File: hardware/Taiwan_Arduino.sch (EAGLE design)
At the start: 44 parts, among them J1 AVR_SPI_PRG_62X3_LOCK, T1 2SC, T2 2N, U1 ATMEGA328P_PDIP, Y2 16mhz

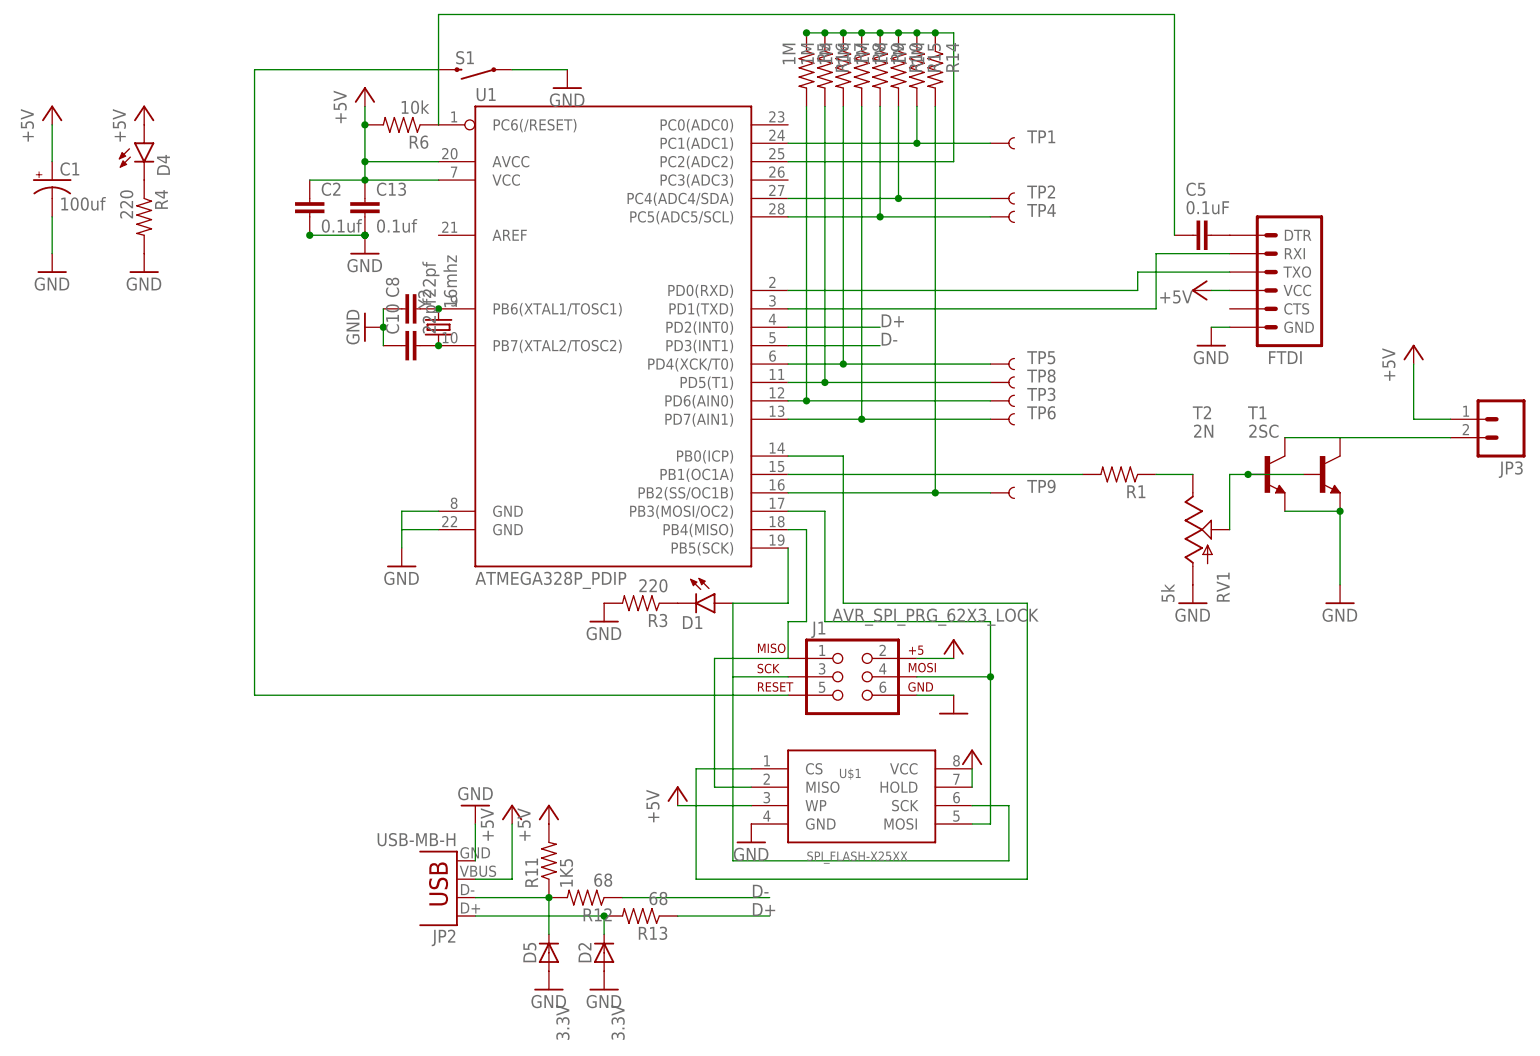
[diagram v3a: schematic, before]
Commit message: Improve touch pad grounding
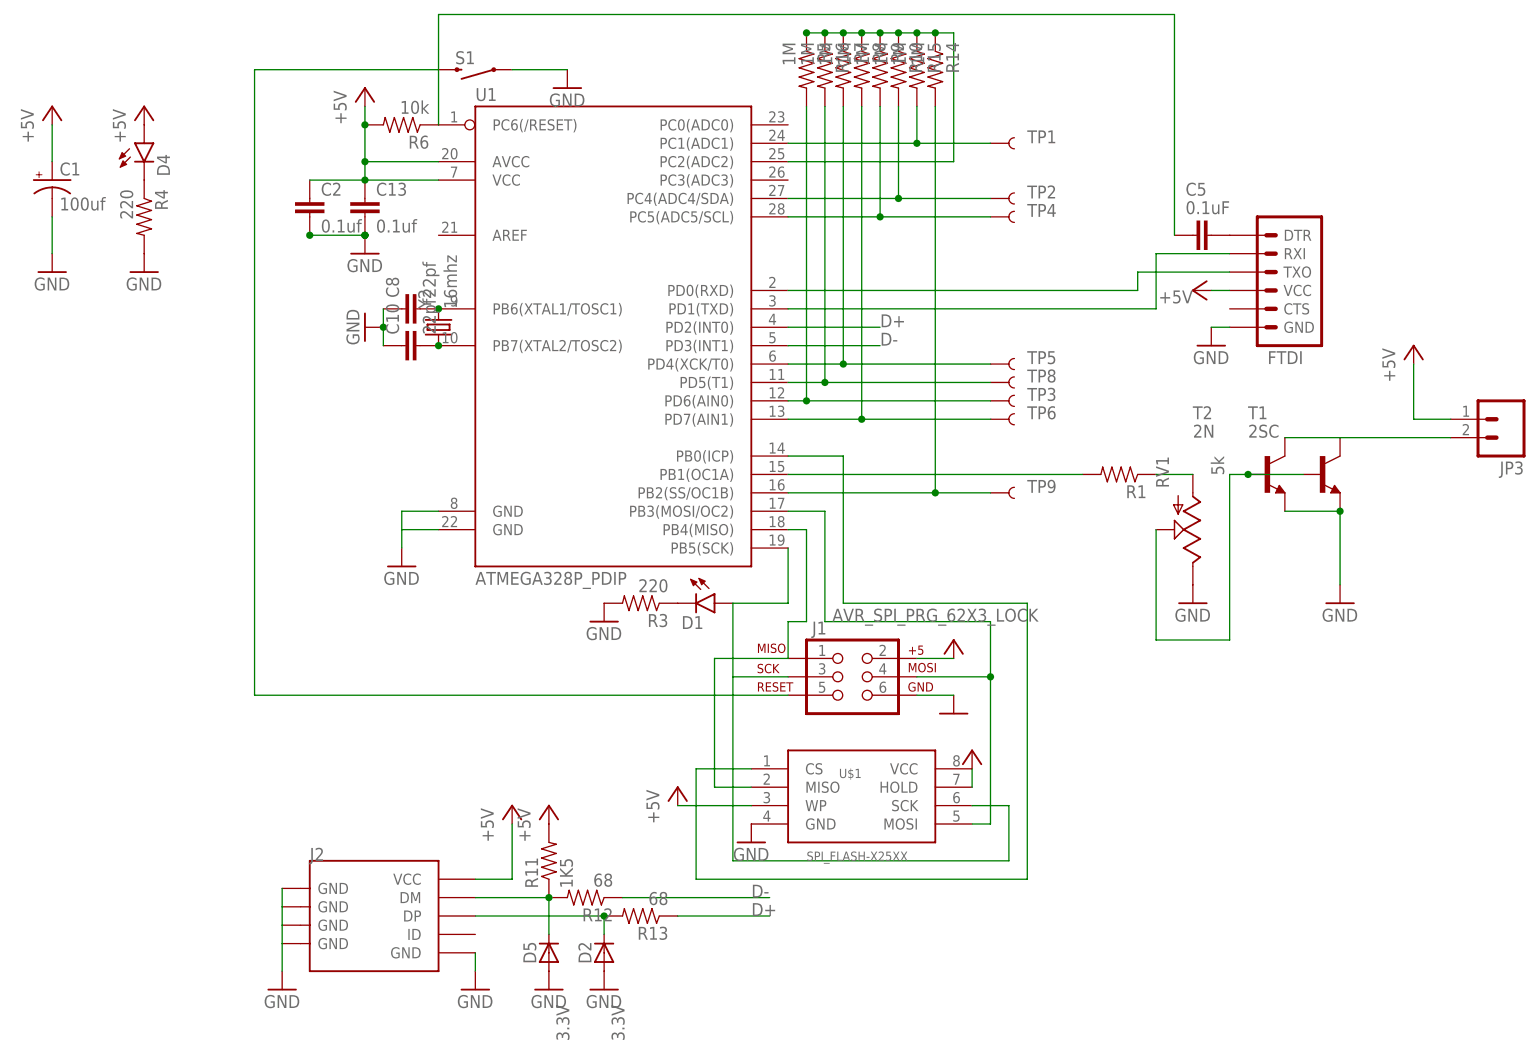
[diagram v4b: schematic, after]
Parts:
- removed JP2: USB-MB-H, SparkFun-Connectors:USB-MB-H
- added J2: (no value), Connector :USB-MINIUSB-5P-TH
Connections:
- net +5V: now also J2.VCC; no longer JP2.VBUS
- net GND: now also J2.GND@1, J2.GND@2, J2.GND@3, J2.GND@4, J2.GND@5, RV1.E; no longer JP2.GND, RV1.A
- net N$1: now also RV1.A; no longer RV1.E
- net N$15: now also J2.DM; no longer JP2.D-
- net N$16: now also J2.DP; no longer JP2.D+
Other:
- moved on the sheet: RV1
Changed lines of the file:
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@@
 <setting verticaltext="up"/>
 </settings>
-<grid distance="0.1" unitdist="inch" unit="inch" style="lines" multiple="1" display="no" altdistance="0.01" altunitdist="inch" altunit="inch"/>
+<grid distance="0.05" unitdist="inch" unit="inch" style="lines" multiple="1" display="no" altdistance="0.01" altunitdist="inch" altunit="inch"/>
 <layers>
 <layer number="1" name="Top" color="4" fill="1" visible="yes" active="no"/>
@@
 <part name="P+11" library="supply1" deviceset="+5V" device=""/>
 <part name="GND22" library="supply1" deviceset="GND" device=""/>
-<part name="JP2" library="SparkFun-Connectors" deviceset="USB" device="-MB-H"/>
 <part name="GND4" library="supply1" deviceset="GND" device=""/>
 <part name="C13" library="SparkFun-Capacitors" deviceset="CAP" device="PTH" value="0.1uf"/>
@@
 <part name="D5" library="_JJG-parts" deviceset="DIODE-VERT" device="DIODE_SM_VERT" value="3.3V"/>
 <part name="D2" library="_JJG-parts" deviceset="DIODE-VERT" device="DIODE_SM_VERT" value="3.3V"/>
+<part name="J2" library="Connector " deviceset="USB-MINIUSB-5P" device="-TH"/>
+<part name="GND1" library="supply1" deviceset="GND" device=""/>
 </parts>
 <sheets>
@@
 <instance part="GND15" gate="1" x="60.96" y="12.7"/>
 <instance part="P+11" gate="1" x="48.26" y="38.1"/>
-<instance part="GND22" gate="1" x="43.18" y="38.1" rot="R180"/>
-<instance part="JP2" gate="G$1" x="40.64" y="30.48" rot="R180"/>
+<instance part="GND22" gate="1" x="43.18" y="12.7"/>
 <instance part="GND4" gate="1" x="33.02" y="71.12"/>
 <instance part="C13" gate="G$1" x="27.94" y="119.38"/>
@@
 <instance part="GND3" gate="1" x="162.56" y="66.04"/>
 <instance part="P+1" gate="1" x="172.72" y="101.6"/>
-<instance part="RV1" gate="G$1" x="142.24" y="76.2"/>
+<instance part="RV1" gate="G$1" x="142.24" y="76.2" rot="R180"/>
 <instance part="GND6" gate="1" x="142.24" y="66.04"/>
 <instance part="U$1" gate="G$1" x="96.52" y="40.64" smashed="yes">
@@
 <attribute name="VALUE" x="63.7794" y="5.588" size="1.778" layer="96" rot="R90"/>
 </instance>
+<instance part="J2" gate="USB" x="29.21" y="22.86"/>
+<instance part="GND1" gate="1" x="16.51" y="12.7"/>
 </instances>
 <busses>
@@
 <nets>
 <net name="GND" class="0">
-<segment>
-<pinref part="GND22" gate="1" pin="GND"/>
-<wire x1="43.18" y1="35.56" x2="43.18" y2="30.48" width="0.1524" layer="91"/>
-<pinref part="JP2" gate="G$1" pin="GND"/>
-</segment>
 <segment>
 <pinref part="C13" gate="G$1" pin="2"/>
@@
 </segment>
 <segment>
-<pinref part="RV1" gate="G$1" pin="A"/>
-<pinref part="GND6" gate="1" pin="GND"/>
-</segment>
-<segment>
 <pinref part="R4" gate="G$1" pin="2"/>
 <pinref part="GND11" gate="1" pin="GND"/>
@@
 <pinref part="D2" gate="1" pin="A"/>
 </segment>
+<segment>
+<pinref part="J2" gate="USB" pin="GND@5"/>
+<pinref part="GND22" gate="1" pin="GND"/>
+<wire x1="43.18" y1="15.24" x2="43.18" y2="17.78" width="0.1524" layer="91"/>
+</segment>
+<segment>
+<pinref part="J2" gate="USB" pin="GND@1"/>
+<pinref part="J2" gate="USB" pin="GND@2"/>
+<wire x1="16.51" y1="26.67" x2="16.51" y2="24.13" width="0.1524" layer="91"/>
+<pinref part="J2" gate="USB" pin="GND@3"/>
+<wire x1="16.51" y1="24.13" x2="16.51" y2="21.59" width="0.1524" layer="91"/>
+<pinref part="J2" gate="USB" pin="GND@4"/>
+<wire x1="16.51" y1="21.59" x2="16.51" y2="19.05" width="0.1524" layer="91"/>
+<pinref part="GND1" gate="1" pin="GND"/>
+<wire x1="16.51" y1="19.05" x2="16.51" y2="15.24" width="0.1524" layer="91"/>
+</segment>
+<segment>
+<pinref part="RV1" gate="G$1" pin="E"/>
+<pinref part="GND6" gate="1" pin="GND"/>
+</segment>
 </net>
 <net name="+5V" class="0">
@@
 <wire x1="43.18" y1="27.94" x2="48.26" y2="27.94" width="0.1524" layer="91"/>
 <wire x1="48.26" y1="27.94" x2="48.26" y2="35.56" width="0.1524" layer="91"/>
-<pinref part="JP2" gate="G$1" pin="VBUS"/>
+<pinref part="J2" gate="USB" pin="VCC"/>
 </segment>
 <segment>
@@
 <junction x="53.34" y="25.4"/>
 <pinref part="R12" gate="G$1" pin="2"/>
-<pinref part="JP2" gate="G$1" pin="D-"/>
 <pinref part="D5" gate="1" pin="C"/>
+<pinref part="J2" gate="USB" pin="DM"/>
 </segment>
 </net>
@@
 <pinref part="R13" gate="G$1" pin="2"/>
 <junction x="60.96" y="22.86"/>
-<pinref part="JP2" gate="G$1" pin="D+"/>
 <pinref part="D2" gate="1" pin="C"/>
+<pinref part="J2" gate="USB" pin="DP"/>
 </segment>
 </net>
@@
 </segment>
 </net>
-<net name="N$1" class="0">
-<segment>
-<pinref part="R1" gate="G$1" pin="1"/>
-<pinref part="RV1" gate="G$1" pin="E"/>
-<wire x1="137.16" y1="83.82" x2="142.24" y2="83.82" width="0.1524" layer="91"/>
-</segment>
-</net>
 <net name="N$2" class="0">
 <segment>
@@
 <net name="N$22" class="0">
 <segment>
-<pinref part="RV1" gate="G$1" pin="S"/>
-<wire x1="147.32" y1="76.2" x2="147.32" y2="83.82" width="0.1524" layer="91"/>
 <pinref part="T1" gate="G$1" pin="B"/>
 <wire x1="157.48" y1="83.82" x2="149.86" y2="83.82" width="0.1524" layer="91"/>
@@
 <wire x1="149.86" y1="83.82" x2="147.32" y2="83.82" width="0.1524" layer="91"/>
 <junction x="149.86" y="83.82"/>
+<wire x1="147.32" y1="83.82" x2="147.32" y2="60.96" width="0.1524" layer="91"/>
+<pinref part="RV1" gate="G$1" pin="S"/>
+<wire x1="147.32" y1="60.96" x2="137.16" y2="60.96" width="0.1524" layer="91"/>
+<wire x1="137.16" y1="60.96" x2="137.16" y2="76.2" width="0.1524" layer="91"/>
 </segment>
 </net>
@@
 </segment>
 </net>
+<net name="N$1" class="0">
+<segment>
+<pinref part="R1" gate="G$1" pin="1"/>
+<pinref part="RV1" gate="G$1" pin="A"/>
+<wire x1="142.24" y1="83.82" x2="137.16" y2="83.82" width="0.1524" layer="91"/>
+</segment>
+</net>

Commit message: Ver 1.0
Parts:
- removed T1: 2SC, transistor:2SC1815
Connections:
- removed net N$18: JP3.2, T1.C, T2.C
- new net N$12: JP3.1, T2.C
- net +5V: now also JP3.2; no longer JP3.1
- net GND: no longer T1.E
- net N$22: no longer T1.B
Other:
- moved on the sheet: JP3
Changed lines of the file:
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@@
 <setting verticaltext="up"/>
 </settings>
-<grid distance="0.05" unitdist="inch" unit="inch" style="lines" multiple="1" display="no" altdistance="0.01" altunitdist="inch" altunit="inch"/>
+<grid distance="0.1" unitdist="inch" unit="inch" style="lines" multiple="1" display="no" altdistance="0.01" altunitdist="inch" altunit="inch"/>
 <layers>
-<layer number="1" name="Top" color="4" fill="1" visible="yes" active="no"/>
-<layer number="16" name="Bottom" color="1" fill="1" visible="yes" active="no"/>
-<layer number="17" name="Pads" color="2" fill="1" visible="yes" active="no"/>
-<layer number="18" name="Vias" color="2" fill="1" visible="yes" active="no"/>
-<layer number="19" name="Unrouted" color="6" fill="1" visible="yes" active="no"/>
-<layer number="20" name="Dimension" color="15" fill="1" visible="yes" active="no"/>
-<layer number="21" name="tPlace" color="7" fill="1" visible="yes" active="no"/>
-<layer number="22" name="bPlace" color="7" fill="1" visible="yes" active="no"/>
-<layer number="23" name="tOrigins" color="15" fill="1" visible="yes" active="no"/>
-<layer number="24" name="bOrigins" color="15" fill="1" visible="yes" active="no"/>
-<layer number="25" name="tNames" color="7" fill="1" visible="yes" active="no"/>
-<layer number="26" name="bNames" color="7" fill="1" visible="yes" active="no"/>
-<layer number="27" name="tValues" color="7" fill="1" visible="yes" active="no"/>
-<layer number="28" name="bValues" color="7" fill="1" visible="yes" active="no"/>
+<layer number="1" name="Top" color="4" fill="1" visible="no" active="no"/>
+<layer number="16" name="Bottom" color="1" fill="1" visible="no" active="no"/>
+<layer number="17" name="Pads" color="2" fill="1" visible="no" active="no"/>
+<layer number="18" name="Vias" color="2" fill="1" visible="no" active="no"/>
+<layer number="19" name="Unrouted" color="6" fill="1" visible="no" active="no"/>
+<layer number="20" name="Dimension" color="15" fill="1" visible="no" active="no"/>
+<layer number="21" name="tPlace" color="7" fill="1" visible="no" active="no"/>
+<layer number="22" name="bPlace" color="7" fill="1" visible="no" active="no"/>
+<layer number="23" name="tOrigins" color="15" fill="1" visible="no" active="no"/>
+<layer number="24" name="bOrigins" color="15" fill="1" visible="no" active="no"/>
+<layer number="25" name="tNames" color="7" fill="1" visible="no" active="no"/>
+<layer number="26" name="bNames" color="7" fill="1" visible="no" active="no"/>
+<layer number="27" name="tValues" color="7" fill="1" visible="no" active="no"/>
+<layer number="28" name="bValues" color="7" fill="1" visible="no" active="no"/>
 <layer number="29" name="tStop" color="7" fill="3" visible="no" active="no"/>
 <layer number="30" name="bStop" color="7" fill="6" visible="no" active="no"/>
@@
 <layer number="35" name="tGlue" color="7" fill="4" visible="no" active="no"/>
 <layer number="36" name="bGlue" color="7" fill="5" visible="no" active="no"/>
-<layer number="37" name="tTest" color="7" fill="1" visible="yes" active="no"/>
-<layer number="38" name="bTest" color="7" fill="1" visible="yes" active="no"/>
+<layer number="37" name="tTest" color="7" fill="1" visible="no" active="no"/>
+<layer number="38" name="bTest" color="7" fill="1" visible="no" active="no"/>
 <layer number="39" name="tKeepout" color="4" fill="11" visible="no" active="no"/>
 <layer number="40" name="bKeepout" color="1" fill="11" visible="no" active="no"/>
@@
 <layer number="44" name="Drills" color="7" fill="1" visible="no" active="no"/>
 <layer number="45" name="Holes" color="7" fill="1" visible="no" active="no"/>
-<layer number="46" name="Milling" color="3" fill="1" visible="yes" active="no"/>
-<layer number="47" name="Measures" color="7" fill="1" visible="yes" active="no"/>
-<layer number="48" name="Document" color="7" fill="1" visible="yes" active="no"/>
-<layer number="49" name="Reference" color="7" fill="1" visible="yes" active="no"/>
-<layer number="50" name="dxf" color="7" fill="1" visible="yes" active="no"/>
-<layer number="51" name="tDocu" color="7" fill="1" visible="yes" active="no"/>
-<layer number="52" name="bDocu" color="7" fill="1" visible="yes" active="no"/>
-<layer number="53" name="tGND_GNDA" color="7" fill="9" visible="yes" active="no"/>
-<layer number="54" name="bGND_GNDA" color="1" fill="9" visible="yes" active="no"/>
-<layer number="56" name="wert" color="7" fill="1" visible="yes" active="no"/>
-<layer number="57" name="tCAD" color="7" fill="1" visible="yes" active="no"/>
-<layer number="59" name="tCarbon" color="7" fill="1" visible="yes" active="no"/>
-<layer number="60" name="bCarbon" color="7" fill="1" visible="yes" active="no"/>
+<layer number="46" name="Milling" color="3" fill="1" visible="no" active="no"/>
+<layer number="47" name="Measures" color="7" fill="1" visible="no" active="no"/>
+<layer number="48" name="Document" color="7" fill="1" visible="no" active="no"/>
+<layer number="49" name="Reference" color="7" fill="1" visible="no" active="no"/>
+<layer number="50" name="dxf" color="7" fill="1" visible="no" active="no"/>
+<layer number="51" name="tDocu" color="7" fill="1" visible="no" active="no"/>
+<layer number="52" name="bDocu" color="7" fill="1" visible="no" active="no"/>
+<layer number="53" name="tGND_GNDA" color="7" fill="9" visible="no" active="no"/>
+<layer number="54" name="bGND_GNDA" color="1" fill="9" visible="no" active="no"/>
+<layer number="56" name="wert" color="7" fill="1" visible="no" active="no"/>
+<layer number="57" name="tCAD" color="7" fill="1" visible="no" active="no"/>
+<layer number="59" name="tCarbon" color="7" fill="1" visible="no" active="no"/>
+<layer number="60" name="bCarbon" color="7" fill="1" visible="no" active="no"/>
 <layer number="90" name="Modules" color="5" fill="1" visible="yes" active="yes"/>
 <layer number="91" name="Nets" color="2" fill="1" visible="yes" active="yes"/>
@@
 <part name="P+8" library="supply1" deviceset="+5V" device=""/>
 <part name="GND18" library="supply1" deviceset="GND" device=""/>
-<part name="T1" library="transistor" deviceset="2SC1815" device="" value="2SC"/>
 <part name="T2" library="adafruit" deviceset="2N2222" device="" value="2N"/>
 <part name="C1" library="adafruit" deviceset="CPOL-US" device="E2.5-5" value="100uf"/>
@@
 <instance part="GND14" gate="1" x="81.28" y="33.02"/>
 <instance part="P+7" gate="1" x="71.12" y="40.64"/>
-<instance part="JP3" gate="G$1" x="185.42" y="91.44" smashed="yes" rot="R180">
-<attribute name="NAME" x="187.96" y="85.598" size="1.778" layer="95" rot="R180"/>
+<instance part="JP3" gate="G$1" x="165.1" y="88.9" smashed="yes">
+<attribute name="NAME" x="162.56" y="94.742" size="1.778" layer="95"/>
 </instance>
 <instance part="R5" gate="G$1" x="88.9" y="139.7" rot="R270"/>
@@
 <instance part="P+8" gate="1" x="-15.24" y="134.62"/>
 <instance part="GND18" gate="1" x="-15.24" y="111.76"/>
-<instance part="T1" gate="G$1" x="160.02" y="83.82"/>
 <instance part="T2" gate="G$1" x="152.4" y="83.82"/>
 <instance part="C1" gate="G$1" x="-15.24" y="124.46"/>
@@
 </segment>
 <segment>
-<pinref part="T1" gate="G$1" pin="E"/>
 <wire x1="154.94" y1="78.74" x2="162.56" y2="78.74" width="0.1524" layer="91"/>
 <pinref part="GND3" gate="1" pin="GND"/>
 <wire x1="162.56" y1="78.74" x2="162.56" y2="68.58" width="0.1524" layer="91"/>
 <pinref part="T2" gate="G$1" pin="E"/>
-<junction x="162.56" y="78.74"/>
 </segment>
 <segment>
@@
 <pinref part="P+1" gate="1" pin="+5V"/>
 <wire x1="172.72" y1="99.06" x2="172.72" y2="91.44" width="0.1524" layer="91"/>
-<pinref part="JP3" gate="G$1" pin="1"/>
-<wire x1="172.72" y1="91.44" x2="177.8" y2="91.44" width="0.1524" layer="91"/>
+<pinref part="JP3" gate="G$1" pin="2"/>
 </segment>
 </net>
@@
 </segment>
 </net>
-<net name="N$18" class="0">
-<segment>
-<pinref part="T1" gate="G$1" pin="C"/>
-<wire x1="154.94" y1="88.9" x2="162.56" y2="88.9" width="0.1524" layer="91"/>
-<pinref part="T2" gate="G$1" pin="C"/>
-<pinref part="JP3" gate="G$1" pin="2"/>
-<wire x1="162.56" y1="88.9" x2="177.8" y2="88.9" width="0.1524" layer="91"/>
-</segment>
-</net>
 <net name="N$22" class="0">
 <segment>
-<pinref part="T1" gate="G$1" pin="B"/>
-<wire x1="157.48" y1="83.82" x2="149.86" y2="83.82" width="0.1524" layer="91"/>
 <pinref part="T2" gate="G$1" pin="B"/>
 <wire x1="149.86" y1="83.82" x2="147.32" y2="83.82" width="0.1524" layer="91"/>
-<junction x="149.86" y="83.82"/>
 <wire x1="147.32" y1="83.82" x2="147.32" y2="60.96" width="0.1524" layer="91"/>
 <pinref part="RV1" gate="G$1" pin="S"/>
@@
 </segment>
 </net>
+<net name="N$12" class="0">
+<segment>
+<pinref part="T2" gate="G$1" pin="C"/>
+<wire x1="154.94" y1="88.9" x2="160.02" y2="88.9" width="0.1524" layer="91"/>
+<wire x1="160.02" y1="88.9" x2="160.02" y2="81.28" width="0.1524" layer="91"/>
+<pinref part="JP3" gate="G$1" pin="1"/>
+<wire x1="160.02" y1="81.28" x2="172.72" y2="81.28" width="0.1524" layer="91"/>
+<wire x1="172.72" y1="81.28" x2="172.72" y2="88.9" width="0.1524" layer="91"/>
+</segment>
+</net>
